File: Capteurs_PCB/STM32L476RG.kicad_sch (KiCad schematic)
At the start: 1 part, among them U2 STM32L476RGTx

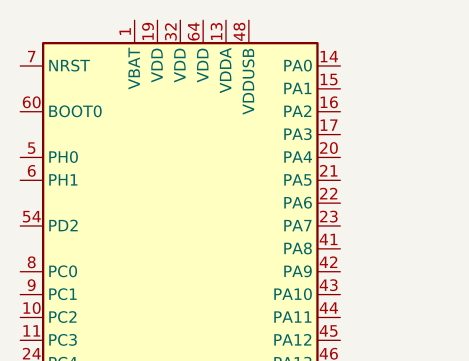
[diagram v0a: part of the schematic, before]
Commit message: PCB changement
Pcb changé (Raspberry))
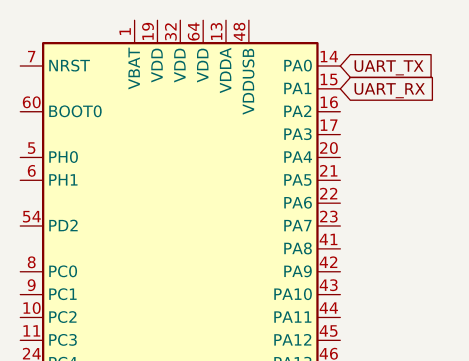
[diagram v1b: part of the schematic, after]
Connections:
- net UART_TX: now reaches U2.14 (PA0)
- net UART_RX: now reaches U2.15 (PA1)
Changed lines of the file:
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@@
 (kicad_sch (version 20230121) (generator eeschema)
   (paper "A4")
+  (global_label "UART_RX" (shape input) (at 157.48 59.69 0) (fields_autoplaced)
+    (effects (font (size 1.27 1.27)) (justify left))
+    (property "Intersheetrefs" "${INTERSHEET_REFS}" (at 168.4896 59.69 0)
+      (effects (font (size 1.27 1.27)) (justify left) hide)
+    )
+  )
+  (global_label "UART_TX" (shape input) (at 157.48 57.15 0) (fields_autoplaced)
+    (effects (font (size 1.27 1.27)) (justify left))
+    (property "Intersheetrefs" "${INTERSHEET_REFS}" (at 168.1872 57.15 0)
+      (effects (font (size 1.27 1.27)) (justify left) hide)
+    )
+  )
   (symbol (lib_id "MCU_ST_STM32L4:STM32L476RGTx") (at 139.7 100.33 0) (unit 1)
     (in_bom yes) (on_board yes) (dnp no) (fields_autoplaced)

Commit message: pcb update
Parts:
- added C8: 100nF, symbol Device:C_Small
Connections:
- net UART_RX: now also U2.52 (PC11); no longer U2.15 (PA1)
- net UART_TX: now also U2.51 (PC10); no longer U2.14 (PA0)
- net Earth: now reaches U2.12 (VSSA)
- net Earth: now also U2.18 (VSS), U2.31 (VSS), U2.47 (VSS), U2.63 (VSS), C8.2
- net V_5V: now reaches U2.19 (VDD)
- net V_5V: now also C8.1
- net SS: now reaches U2.20 (PA4)
- net SCLK: now reaches U2.21 (PA5)
- net MISO: now reaches U2.22 (PA6)
- net MOSI: now reaches U2.23 (PA7)
- net CS: now reaches U2.35 (PB14)
- net SDX: now reaches U2.36 (PB15)
- new net INT1: U2.14 (PA0)
- new net INT2: U2.15 (PA1)
- no-connect marks 0 -> 43
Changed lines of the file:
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@@
 (kicad_sch (version 20230121) (generator eeschema)
   (paper "A4")
-  (global_label "UART_RX" (shape input) (at 157.48 59.69 0) (fields_autoplaced)
-    (effects (font (size 1.27 1.27)) (justify left))
-    (property "Intersheetrefs" "${INTERSHEET_REFS}" (at 168.4896 59.69 0)
-      (effects (font (size 1.27 1.27)) (justify left) hide)
-    )
-  )
-  (global_label "UART_TX" (shape input) (at 157.48 57.15 0) (fields_autoplaced)
-    (effects (font (size 1.27 1.27)) (justify left))
-    (property "Intersheetrefs" "${INTERSHEET_REFS}" (at 168.1872 57.15 0)
+  (junction (at 137.16 46.99) (diameter 0) (color 0 0 0 0)
+  )
+  (junction (at 140.97 146.05) (diameter 0) (color 0 0 0 0)
+  )
+  (no_connect (at 121.92 118.11))
+  (no_connect (at 121.92 82.55))
+  (no_connect (at 121.92 74.93))
+  (no_connect (at 121.92 102.87))
+  (no_connect (at 121.92 100.33))
+  (no_connect (at 157.48 102.87))
+  (no_connect (at 157.48 92.71))
+  (no_connect (at 157.48 87.63))
+  (no_connect (at 157.48 125.73))
+  (no_connect (at 157.48 95.25))
+  (no_connect (at 157.48 118.11))
+  (no_connect (at 121.92 95.25))
+  (no_connect (at 157.48 77.47))
+  (no_connect (at 157.48 107.95))
+  (no_connect (at 121.92 85.09))
+  (no_connect (at 121.92 115.57))
+  (no_connect (at 121.92 113.03))
+  (no_connect (at 157.48 100.33))
+  (no_connect (at 121.92 69.85))
+  (no_connect (at 157.48 113.03))
+  (no_connect (at 121.92 87.63))
+  (no_connect (at 121.92 110.49))
+  (no_connect (at 121.92 57.15))
+  (no_connect (at 157.48 128.27))
+  (no_connect (at 157.48 123.19))
+  (no_connect (at 157.48 90.17))
+  (no_connect (at 121.92 97.79))
+  (no_connect (at 157.48 133.35))
+  (no_connect (at 157.48 130.81))
+  (no_connect (at 121.92 62.23))
+  (no_connect (at 157.48 105.41))
+  (no_connect (at 121.92 80.01))
+  (no_connect (at 157.48 80.01))
+  (no_connect (at 157.48 115.57))
+  (no_connect (at 157.48 64.77))
+  (no_connect (at 157.48 85.09))
+  (no_connect (at 121.92 90.17))
+  (no_connect (at 121.92 67.31))
+  (no_connect (at 157.48 120.65))
+  (no_connect (at 121.92 92.71))
+  (no_connect (at 157.48 62.23))
+  (no_connect (at 157.48 110.49))
+  (no_connect (at 157.48 82.55))
+  (wire (pts (xy 140.97 146.05) (xy 142.24 146.05))
+    (stroke (width 0) (type default))
+  )
+  (wire (pts (xy 139.7 146.05) (xy 140.97 146.05))
+    (stroke (width 0) (type default))
+  )
+  (wire (pts (xy 137.16 46.99) (xy 137.16 52.07))
+    (stroke (width 0) (type default))
+  )
+  (wire (pts (xy 137.16 40.64) (xy 137.16 46.99))
+    (stroke (width 0) (type default))
+  )
+  (global_label "INT1" (shape input) (at 157.48 57.15 0) (fields_autoplaced)
+    (effects (font (size 1.27 1.27)) (justify left))
+    (property "Intersheetrefs" "${INTERSHEET_REFS}" (at 164.4982 57.15 0)
+      (effects (font (size 1.27 1.27)) (justify left) hide)
+    )
+  )
+  (global_label "INT2" (shape input) (at 157.48 59.69 0) (fields_autoplaced)
+    (effects (font (size 1.27 1.27)) (justify left))
+    (property "Intersheetrefs" "${INTERSHEET_REFS}" (at 164.4982 59.69 0)
+      (effects (font (size 1.27 1.27)) (justify left) hide)
+    )
+  )
+  (global_label "SDX" (shape input) (at 157.48 138.43 0) (fields_autoplaced)
+    (effects (font (size 1.27 1.27)) (justify left))
+    (property "Intersheetrefs" "${INTERSHEET_REFS}" (at 164.0748 138.43 0)
+      (effects (font (size 1.27 1.27)) (justify left) hide)
+    )
+  )
+  (global_label "UART_RX" (shape input) (at 121.92 107.95 180) (fields_autoplaced)
+    (effects (font (size 1.27 1.27)) (justify right))
+    (property "Intersheetrefs" "${INTERSHEET_REFS}" (at 110.9104 107.95 0)
+      (effects (font (size 1.27 1.27)) (justify right) hide)
+    )
+  )
+  (global_label "CS" (shape input) (at 157.48 135.89 0) (fields_autoplaced)
+    (effects (font (size 1.27 1.27)) (justify left))
+    (property "Intersheetrefs" "${INTERSHEET_REFS}" (at 162.8653 135.89 0)
+      (effects (font (size 1.27 1.27)) (justify left) hide)
+    )
+  )
+  (global_label "UART_TX" (shape input) (at 121.92 105.41 180) (fields_autoplaced)
+    (effects (font (size 1.27 1.27)) (justify right))
+    (property "Intersheetrefs" "${INTERSHEET_REFS}" (at 111.2128 105.41 0)
+      (effects (font (size 1.27 1.27)) (justify right) hide)
+    )
+  )
+  (global_label "V_5V" (shape input) (at 137.16 40.64 90) (fields_autoplaced)
+    (effects (font (size 1.27 1.27)) (justify left))
+    (property "Intersheetrefs" "${INTERSHEET_REFS}" (at 137.16 33.3799 90)
+      (effects (font (size 1.27 1.27)) (justify left) hide)
+    )
+  )
+  (global_label "SCLK" (shape input) (at 157.48 69.85 0) (fields_autoplaced)
+    (effects (font (size 1.27 1.27)) (justify left))
+    (property "Intersheetrefs" "${INTERSHEET_REFS}" (at 165.1634 69.85 0)
+      (effects (font (size 1.27 1.27)) (justify left) hide)
+    )
+  )
+  (global_label "MOSI" (shape input) (at 157.48 74.93 0) (fields_autoplaced)
+    (effects (font (size 1.27 1.27)) (justify left))
+    (property "Intersheetrefs" "${INTERSHEET_REFS}" (at 164.982 74.93 0)
+      (effects (font (size 1.27 1.27)) (justify left) hide)
+    )
+  )
+  (global_label "MISO" (shape input) (at 157.48 72.39 0) (fields_autoplaced)
+    (effects (font (size 1.27 1.27)) (justify left))
+    (property "Intersheetrefs" "${INTERSHEET_REFS}" (at 164.982 72.39 0)
+      (effects (font (size 1.27 1.27)) (justify left) hide)
+    )
+  )
+  (global_label "SS" (shape input) (at 157.48 67.31 0) (fields_autoplaced)
+    (effects (font (size 1.27 1.27)) (justify left))
+    (property "Intersheetrefs" "${INTERSHEET_REFS}" (at 162.8048 67.31 0)
       (effects (font (size 1.27 1.27)) (justify left) hide)
     )
@@
         )
       )
+    )
+  )
+  (symbol (lib_id "power:Earth") (at 142.24 46.99 90) (unit 1)
+    (in_bom yes) (on_board yes) (dnp no) (fields_autoplaced)
+    (property "Reference" "#PWR06" (at 148.59 46.99 0)
+      (effects (font (size 1.27 1.27)) hide)
+    )
+    (property "Value" "Earth" (at 146.05 46.99 0)
+      (effects (font (size 1.27 1.27)) hide)
+    )
+    (property "Footprint" "" (at 142.24 46.99 0)
+      (effects (font (size 1.27 1.27)) hide)
+    )
+    (property "Datasheet" "~" (at 142.24 46.99 0)
+      (effects (font (size 1.27 1.27)) hide)
+    )
+    (pin "1")
+    (instances
+      (project "Capteurs_PCB"
+        (path "/1101af8f-9425-4102-9245-339dc54562bf/484fed71-765a-4020-a5ac-867b14a93f63"
+          (reference "#PWR06") (unit 1)
+        )
+      )
+    )
+  )
+  (symbol (lib_id "Device:C_Small") (at 139.7 46.99 90) (unit 1)
+    (in_bom yes) (on_board yes) (dnp no) (fields_autoplaced)
+    (property "Reference" "C8" (at 139.7063 41.91 90)
+      (effects (font (size 1.27 1.27)))
+    )
+    (property "Value" "100nF" (at 139.7063 44.45 90)
+      (effects (font (size 1.27 1.27)))
+    )
+    (property "Footprint" "" (at 139.7 46.99 0)
+      (effects (font (size 1.27 1.27)) hide)
+    )
+    (property "Datasheet" "~" (at 139.7 46.99 0)
+      (effects (font (size 1.27 1.27)) hide)
+    )
+    (pin "1")
+    (pin "2")
+    (instances
+      (project "Capteurs_PCB"
+        (path "/1101af8f-9425-4102-9245-339dc54562bf/484fed71-765a-4020-a5ac-867b14a93f63"
+          (reference "C8") (unit 1)
+        )
+      )
+    )
+  )
+  (symbol (lib_id "power:Earth") (at 140.97 146.05 0) (unit 1)
+    (in_bom yes) (on_board yes) (dnp no) (fields_autoplaced)
+    (property "Reference" "#PWR08" (at 140.97 152.4 0)
+      (effects (font (size 1.27 1.27)) hide)
+    )
+    (property "Value" "Earth" (at 140.97 149.86 0)
+      (effects (font (size 1.27 1.27)) hide)
+    )
+    (property "Footprint" "" (at 140.97 146.05 0)
+      (effects (font (size 1.27 1.27)) hide)
+    )
+    (property "Datasheet" "~" (at 140.97 146.05 0)
+      (effects (font (size 1.27 1.27)) hide)
+    )
+    (pin "1")
+    (instances
+      (project "Capteurs_PCB"
+        (path "/1101af8f-9425-4102-9245-339dc54562bf/484fed71-765a-4020-a5ac-867b14a93f63"
+          (reference "#PWR08") (unit 1)
+        )
+      )

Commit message: uptdate PCB
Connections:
- net SigProp1: now reaches U2.56 (PB4)
- net SigProp2: now reaches U2.58 (PB6)
- no-connect marks 43 -> 41
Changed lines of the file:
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@@
   (no_connect (at 121.92 80.01))
   (no_connect (at 157.48 80.01))
-  (no_connect (at 157.48 115.57))
   (no_connect (at 157.48 64.77))
   (no_connect (at 157.48 85.09))
@@
   (no_connect (at 121.92 92.71))
   (no_connect (at 157.48 62.23))
-  (no_connect (at 157.48 110.49))
   (no_connect (at 157.48 82.55))
   (wire (pts (xy 140.97 146.05) (xy 142.24 146.05))
@@
     (effects (font (size 1.27 1.27)) (justify left))
     (property "Intersheetrefs" "${INTERSHEET_REFS}" (at 164.4982 57.15 0)
+      (effects (font (size 1.27 1.27)) (justify left) hide)
+    )
+  )
+  (global_label "SigProp1" (shape input) (at 157.48 110.49 0) (fields_autoplaced)
+    (effects (font (size 1.27 1.27)) (justify left))
+    (property "Intersheetrefs" "${INTERSHEET_REFS}" (at 168.9128 110.49 0)
       (effects (font (size 1.27 1.27)) (justify left) hide)
     )
@@
       (effects (font (size 1.27 1.27)) (justify left) hide)
     )
+  )
+  (global_label "SigProp2" (shape input) (at 157.48 115.57 0) (fields_autoplaced)
+    (effects (font (size 1.27 1.27)) (justify left))
+    (property "Intersheetrefs" "${INTERSHEET_REFS}" (at 168.9128 115.57 0)
+      (effects (font (size 1.27 1.27)) (justify left) hide)
+    )

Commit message: updates pcb
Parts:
- C8: footprint (none) -> Capacitor_SMD:C_1206_3216Metric
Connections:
- net FWD1: now reaches U2.16 (PA2)
- net REV1: now reaches U2.17 (PA3)
- net FWD2: now reaches U2.41 (PA8)
- net REV2: now reaches U2.42 (PA9)
- net Sig_LED: now reaches U2.43 (PA10)
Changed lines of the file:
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@@
   (no_connect (at 121.92 118.11))
   (no_connect (at 121.92 82.55))
+  (no_connect (at 142.24 52.07))
   (no_connect (at 121.92 74.93))
   (no_connect (at 121.92 102.87))
@@
   (no_connect (at 157.48 118.11))
   (no_connect (at 121.92 95.25))
-  (no_connect (at 157.48 77.47))
   (no_connect (at 157.48 107.95))
   (no_connect (at 121.92 85.09))
@@
   (no_connect (at 121.92 69.85))
   (no_connect (at 157.48 113.03))
+  (no_connect (at 144.78 52.07))
   (no_connect (at 121.92 87.63))
   (no_connect (at 121.92 110.49))
+  (no_connect (at 134.62 52.07))
   (no_connect (at 121.92 57.15))
   (no_connect (at 157.48 128.27))
@@
   (no_connect (at 157.48 133.35))
   (no_connect (at 157.48 130.81))
+  (no_connect (at 139.7 52.07))
   (no_connect (at 121.92 62.23))
   (no_connect (at 157.48 105.41))
   (no_connect (at 121.92 80.01))
-  (no_connect (at 157.48 80.01))
-  (no_connect (at 157.48 64.77))
   (no_connect (at 157.48 85.09))
   (no_connect (at 121.92 90.17))
   (no_connect (at 121.92 67.31))
   (no_connect (at 157.48 120.65))
+  (no_connect (at 147.32 52.07))
   (no_connect (at 121.92 92.71))
-  (no_connect (at 157.48 62.23))
-  (no_connect (at 157.48 82.55))
   (wire (pts (xy 140.97 146.05) (xy 142.24 146.05))
     (stroke (width 0) (type default))
@@
     (effects (font (size 1.27 1.27)) (justify left))
     (property "Intersheetrefs" "${INTERSHEET_REFS}" (at 164.0748 138.43 0)
+      (effects (font (size 1.27 1.27)) (justify left) hide)
+    )
+  )
+  (global_label "FWD1" (shape input) (at 157.48 62.23 0) (fields_autoplaced)
+    (effects (font (size 1.27 1.27)) (justify left))
+    (property "Intersheetrefs" "${INTERSHEET_REFS}" (at 165.4053 62.23 0)
       (effects (font (size 1.27 1.27)) (justify left) hide)
     )
@@
     )
   )
+  (global_label "Sig_LED" (shape input) (at 157.48 82.55 0) (fields_autoplaced)
+    (effects (font (size 1.27 1.27)) (justify left))
+    (property "Intersheetrefs" "${INTERSHEET_REFS}" (at 167.7638 82.55 0)
+      (effects (font (size 1.27 1.27)) (justify left) hide)
+    )
+  )
   (global_label "CS" (shape input) (at 157.48 135.89 0) (fields_autoplaced)
     (effects (font (size 1.27 1.27)) (justify left))
     (property "Intersheetrefs" "${INTERSHEET_REFS}" (at 162.8653 135.89 0)
+      (effects (font (size 1.27 1.27)) (justify left) hide)
+    )
+  )
+  (global_label "FWD2" (shape input) (at 157.48 77.47 0) (fields_autoplaced)
+    (effects (font (size 1.27 1.27)) (justify left))
+    (property "Intersheetrefs" "${INTERSHEET_REFS}" (at 165.4053 77.47 0)
       (effects (font (size 1.27 1.27)) (justify left) hide)
     )
@@
     )
   )
+  (global_label "REV1" (shape input) (at 157.48 64.77 0) (fields_autoplaced)
+    (effects (font (size 1.27 1.27)) (justify left))
+    (property "Intersheetrefs" "${INTERSHEET_REFS}" (at 165.1029 64.77 0)
+      (effects (font (size 1.27 1.27)) (justify left) hide)
+    )
+  )
   (global_label "SCLK" (shape input) (at 157.48 69.85 0) (fields_autoplaced)
     (effects (font (size 1.27 1.27)) (justify left))
@@
     (effects (font (size 1.27 1.27)) (justify left))
     (property "Intersheetrefs" "${INTERSHEET_REFS}" (at 162.8048 67.31 0)
+      (effects (font (size 1.27 1.27)) (justify left) hide)
+    )
+  )
+  (global_label "REV2" (shape input) (at 157.48 80.01 0) (fields_autoplaced)
+    (effects (font (size 1.27 1.27)) (justify left))
+    (property "Intersheetrefs" "${INTERSHEET_REFS}" (at 165.1029 80.01 0)
       (effects (font (size 1.27 1.27)) (justify left) hide)
     )
@@
       (effects (font (size 1.27 1.27)))
     )
-    (property "Footprint" "" (at 139.7 46.99 0)
-      (effects (font (size 1.27 1.27)) hide)
-    )
+    (property "Footprint" "Capacitor_SMD:C_1206_3216Metric" (at 139.7 46.99 0)
+      (effects (font (size 1.27 1.27)) hide)
+    )
